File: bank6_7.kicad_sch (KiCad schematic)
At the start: 1 part, among them U1 ECP5-BGA256

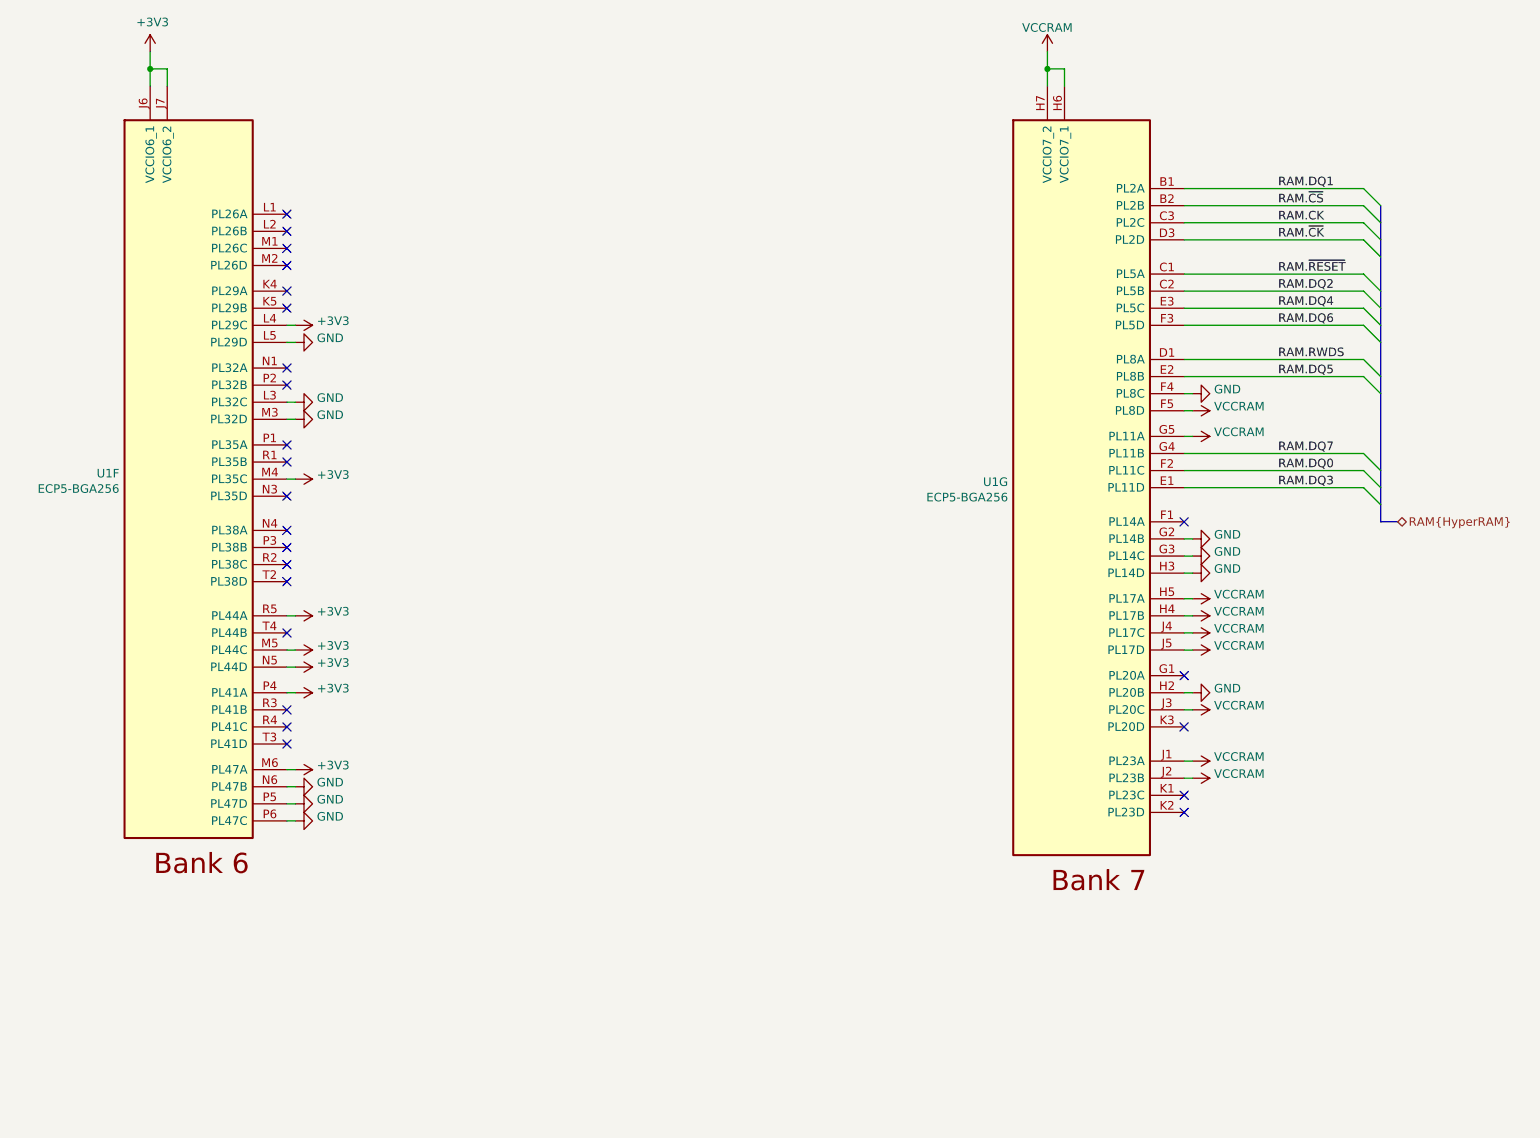
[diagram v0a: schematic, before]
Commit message: Add radio transceiver
Remove Cynthion-specific features
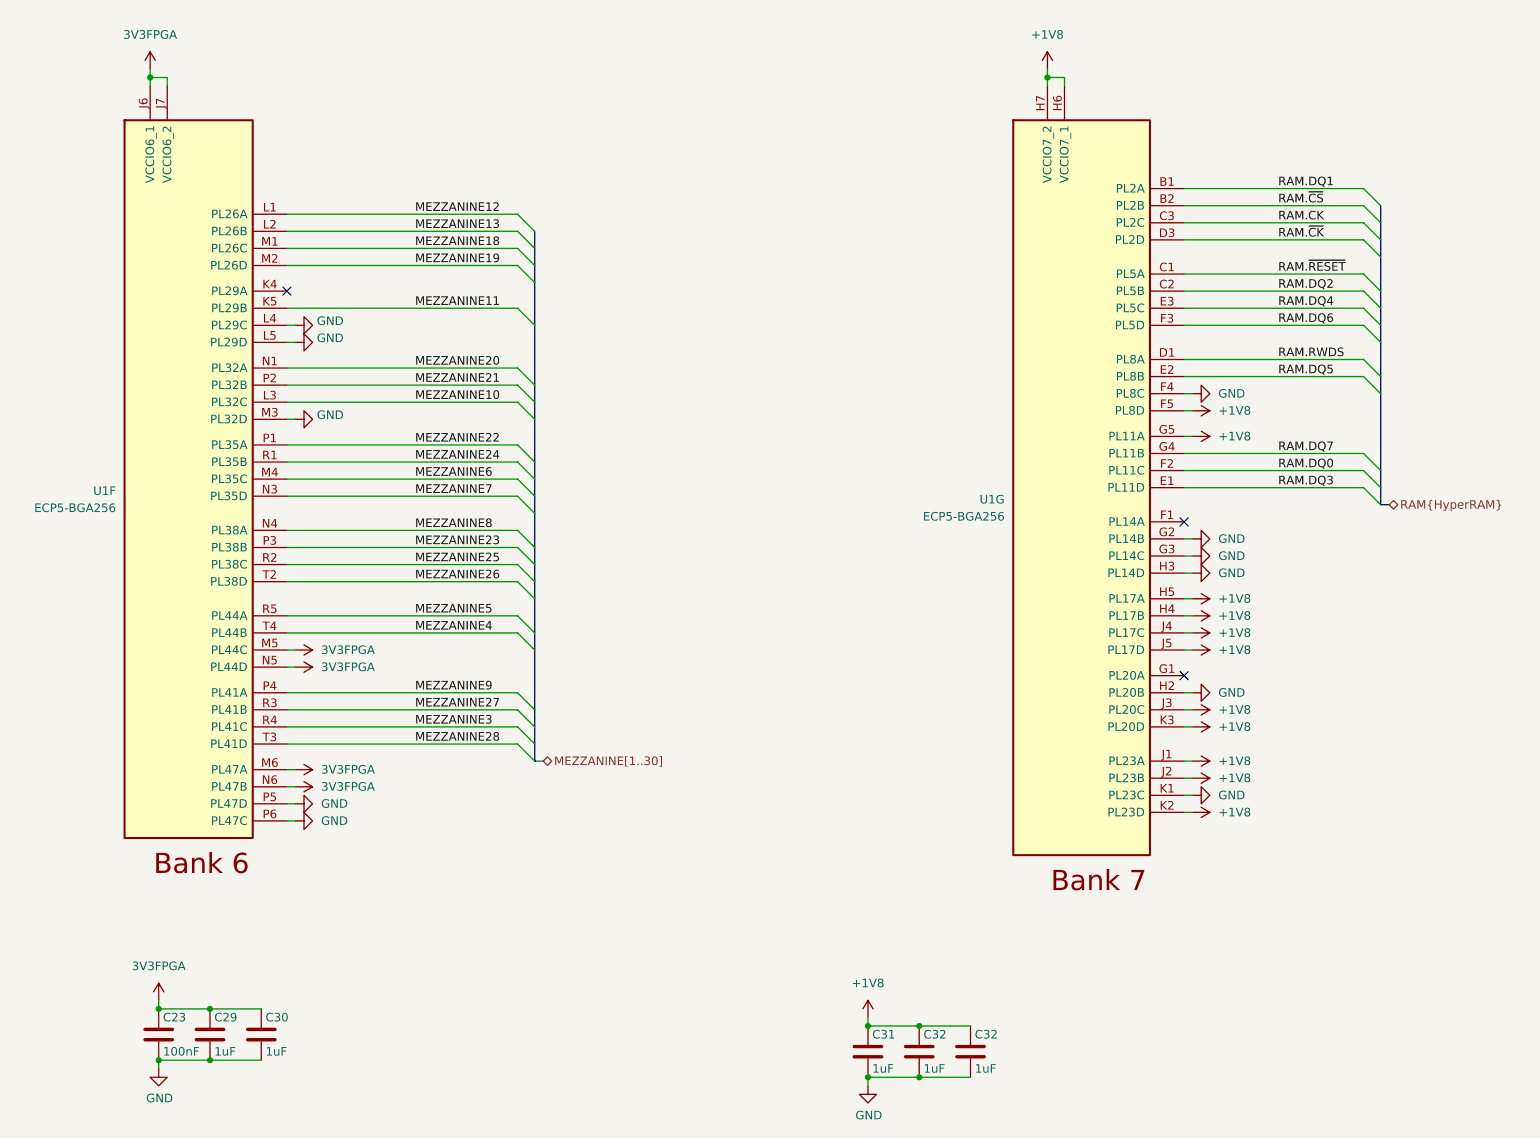
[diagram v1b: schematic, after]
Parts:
- added C23: 100nF, Capacitor_SMD:C_0402_1005Metric, symbol Device:C
- added C29, C30, C31, C32 (x2): 1uF, Capacitor_SMD:C_0402_1005Metric, symbol Device:C
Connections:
- net VCCRAM is gone; now on net +1V8: U1.F5 (PL8D), U1.G5 (PL11A), U1.H4 (PL17B), U1.H5 (PL17A), U1.H6 (VCCIO7_1), U1.H7 (VCCIO7_2), U1.J1 (PL23A), U1.J2 (PL23B), U1.J3 (PL20C), U1.J4 (PL17C), U1.J5 (PL17D)
- net GND: now also U1.K1 (PL23C), U1.L4 (PL29C), C23.2, C29.2, C30.2, C31.2, C32.2, C32.2; no longer U1.L3 (PL32C), U1.N6 (PL47B)
- net MEZZANINE11: now reaches U1.K5 (PL29B)
- net MEZZANINE12: now reaches U1.L1 (PL26A)
- net MEZZANINE13: now reaches U1.L2 (PL26B)
- net MEZZANINE18: now reaches U1.M1 (PL26C)
- net MEZZANINE19: now reaches U1.M2 (PL26D)
- net MEZZANINE20: now reaches U1.N1 (PL32A)
- net MEZZANINE7: now reaches U1.N3 (PL35D)
- net MEZZANINE8: now reaches U1.N4 (PL38A)
- net MEZZANINE22: now reaches U1.P1 (PL35A)
- net MEZZANINE21: now reaches U1.P2 (PL32B)
- net MEZZANINE23: now reaches U1.P3 (PL38B)
- net MEZZANINE24: now reaches U1.R1 (PL35B)
- net MEZZANINE25: now reaches U1.R2 (PL38C)
- net MEZZANINE27: now reaches U1.R3 (PL41B)
- net MEZZANINE3: now reaches U1.R4 (PL41C)
- net MEZZANINE26: now reaches U1.T2 (PL38D)
- net MEZZANINE28: now reaches U1.T3 (PL41D)
- net MEZZANINE4: now reaches U1.T4 (PL44B)
- net +1V8: now reaches U1.K2 (PL23D)
- net +1V8: now also U1.K3 (PL20D), C31.1, C32.1, C32.1
- net +3V3 renamed 3V3FPGA
- net 3V3FPGA: now also U1.N6 (PL47B), C23.1, C29.1, C30.1; no longer U1.L4 (PL29C), U1.M4 (PL35C), U1.P4 (PL41A), U1.R5 (PL44A)
- new net MEZZANINE10: U1.L3 (PL32C)
- new net MEZZANINE5: U1.R5 (PL44A)
- new net MEZZANINE6: U1.M4 (PL35C)
- new net MEZZANINE9: U1.P4 (PL41A)
- no-connect marks 24 -> 3
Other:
- company: Copyright 2023 Great Scott Gadgets -> ${COPYRIGHT}
- title: URTI Mainboard -> ${TITLE}

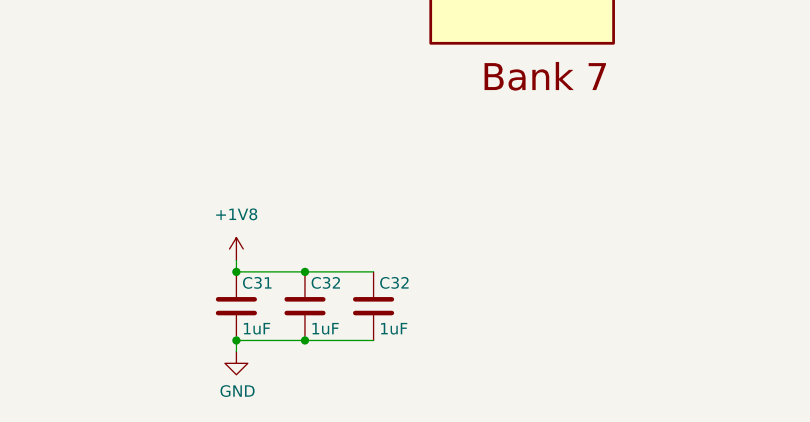
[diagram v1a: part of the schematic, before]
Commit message: Replace open drain clock inverters with push-pull
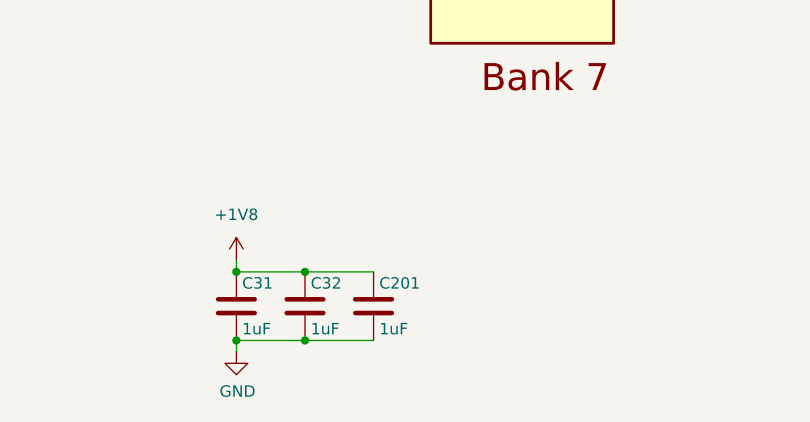
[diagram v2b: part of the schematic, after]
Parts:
- renumbered C32 to C201
